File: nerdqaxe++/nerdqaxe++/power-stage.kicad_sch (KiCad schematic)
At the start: 25 parts, among them U9 CSD95472Q5MC

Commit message: Powermining revision
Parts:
- L2: renamed from L5; value 220nH -> 180nH; OrderNr 283-FP1008R5-R220-RCT-ND -> PA5187.181HLT; PARTNO FP1008R5-R220-R -> PA5187.181HLT
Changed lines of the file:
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@@
 		(on_board yes)
 		(dnp no)
-		(property "Reference" "L5"
+		(property "Reference" "L2"
 			(at 161.29 104.14 90)
 			(effects
@@
 			)
 		)
-		(property "Value" "220nH"
+		(property "Value" "180nH"
 			(at 160.655 107.315 90)
 			(effects
@@
 			)
 		)
-		(property "OrderNr" "283-FP1008R5-R220-RCT-ND"
+		(property "OrderNr" "PA5187.181HLT"
 			(at 160.655 106.045 0)
 			(effects
@@
 			)
 		)
-		(property "PARTNO" "FP1008R5-R220-R"
+		(property "PARTNO" "PA5187.181HLT"
 			(at 160.655 106.045 0)
 			(effects
@@
 				)
 				(path "/e63e39d7-6ac0-4ffd-8aa3-1841a4541b55/8ec0a9c6-2b78-44ef-a83d-9047d2828409/c933835e-1a0a-497e-8f3e-ff83bdc9b421"
-					(reference "L5")
+					(reference "L2")
 					(unit 1)
 				)
 				(path "/e63e39d7-6ac0-4ffd-8aa3-1841a4541b55/8ec0a9c6-2b78-44ef-a83d-9047d2828409/d87aafbc-5a0c-4aaa-b7ac-e134d88b6462"
-					(reference "L6")
+					(reference "L3")
 					(unit 1)
 				)

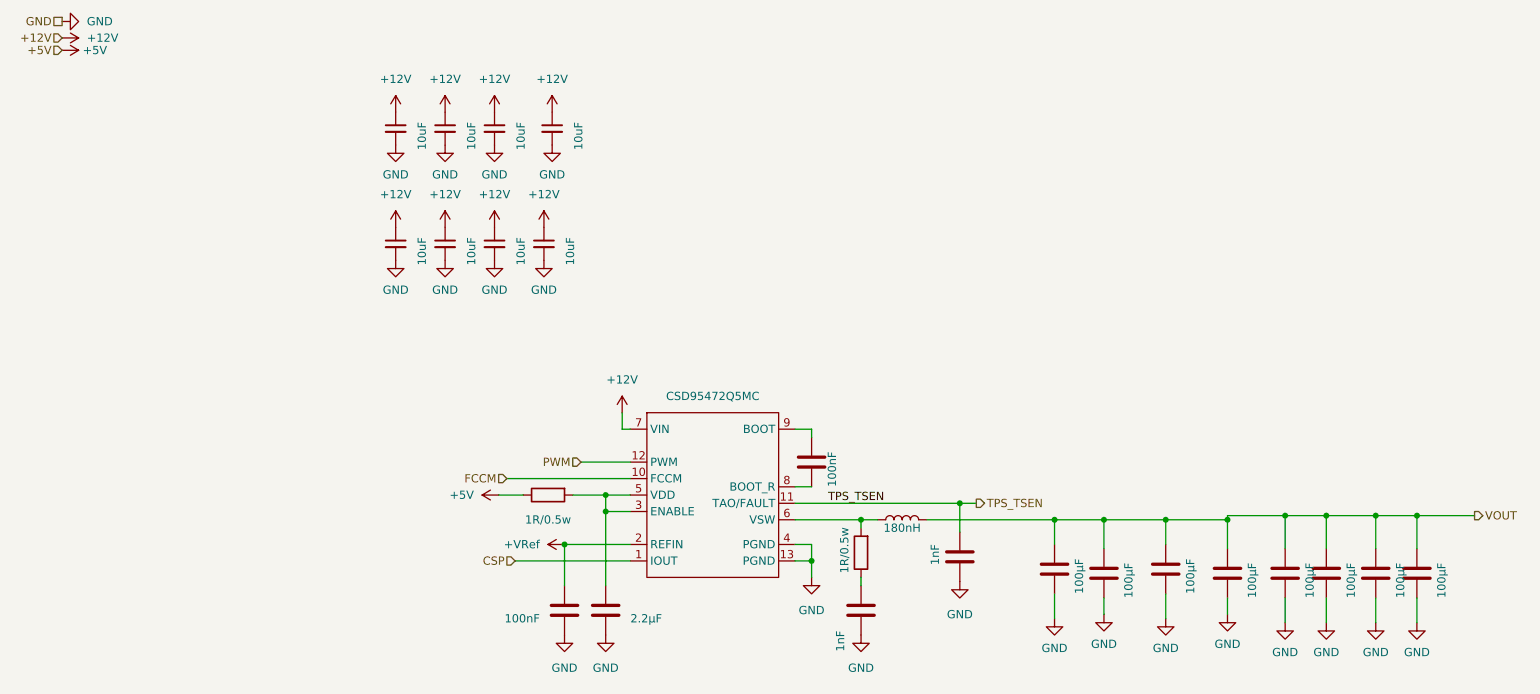
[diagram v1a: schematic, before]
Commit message: Edit on rev 6.1PM
- Moved XT30 connector to the back of the board
- Edited VDD polygon
- Fixed various via placements
- Fixed various tracing
- Updated BM1370 footprint and solder paste stencil
- Updated CSD95472Q5MC footprint and solder paste stencil
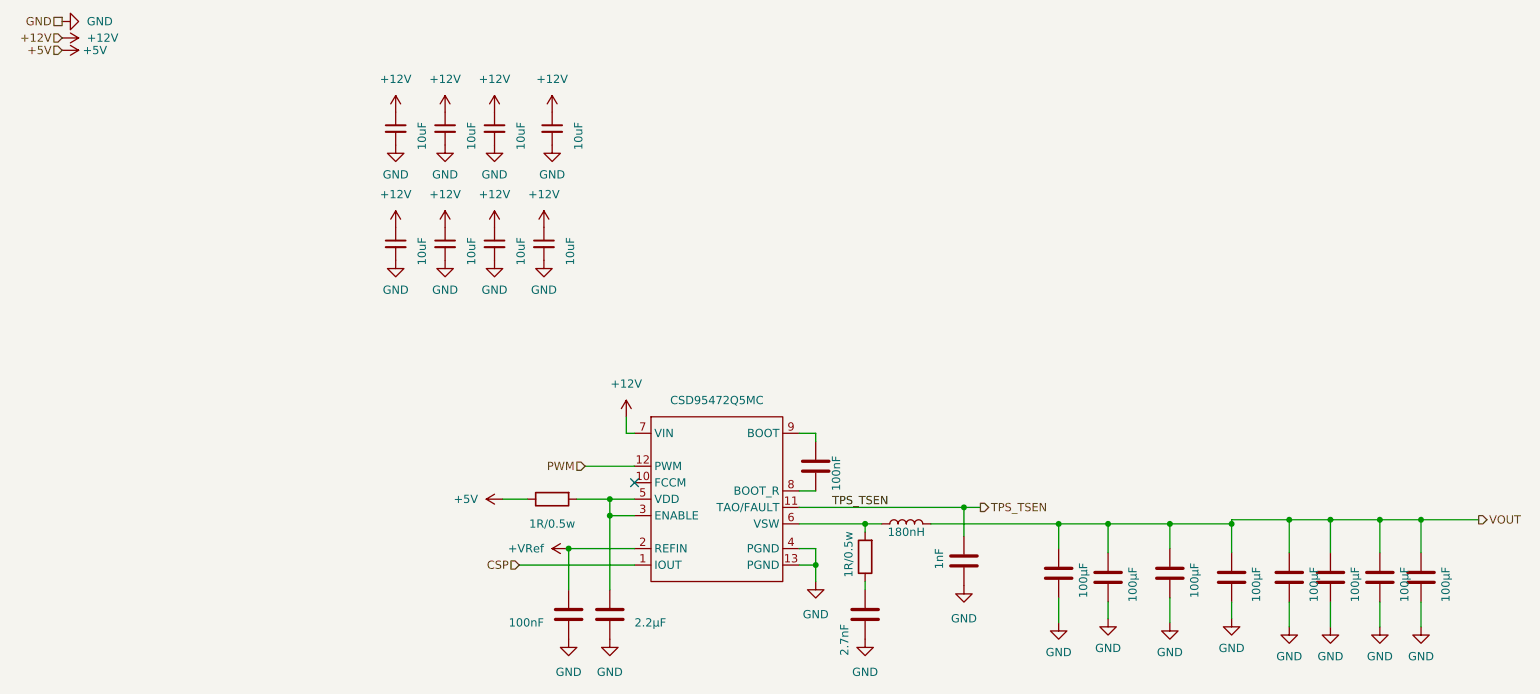
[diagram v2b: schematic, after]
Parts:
- C149: value 1nF -> 2.7nF; LCSC C106205 -> C327272; PARTNO CC0402KRX7R9BB102 -> CC0402JRX7R9BB272
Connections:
- net FCCM: no longer names the net of U9.10 (FCCM)
- no-connect marks 0 -> 1
